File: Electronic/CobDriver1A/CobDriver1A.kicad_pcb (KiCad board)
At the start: 2 copper layers, 15 x 10 mm, 9 parts, among them J1 Conn02_Pin, J2 Conn02_Pin, U1 AL8860WT-7

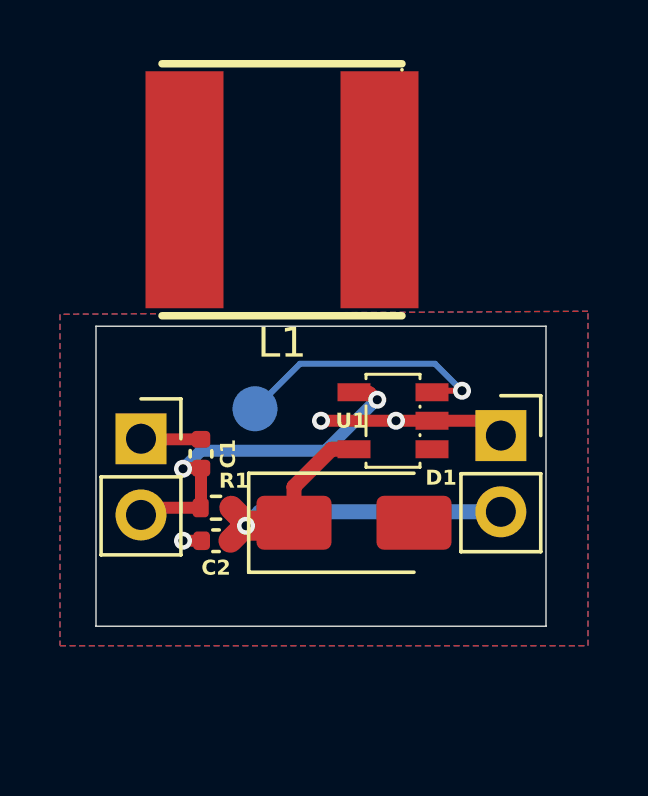
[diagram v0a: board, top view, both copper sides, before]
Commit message: CobDriver1A done
- Smaller inductor
- Bigger PCB
- BOM completed
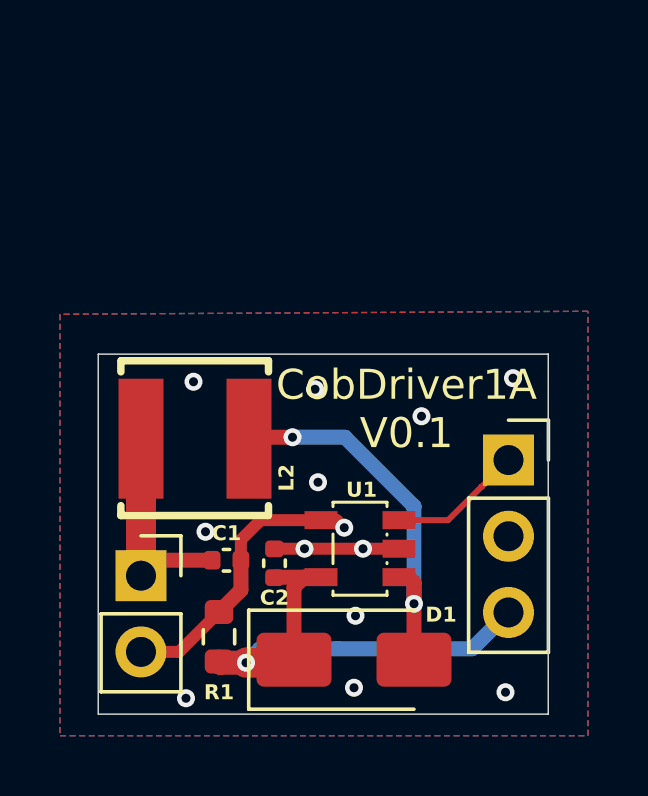
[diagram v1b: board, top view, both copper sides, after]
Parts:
- removed J2: Conn02_Pin, Connector_PinSocket_2.54mm:PinSocket_1x02_P2.54mm_Vertical
- removed L1: ABG08A40M560, lcsc:IND-SMD_L8.0-W8.0_ABG08A40
- removed TP1: TestPoint, TestPoint:TestPoint_Pad_D1.5mm
- added J3: Conn_01x03_Pin, Connector_PinSocket_2.54mm:PinSocket_1x03_P2.54mm_Vertical, F.Cu at (120.8, 60.0)
- added L2: LSXND5050YKL330MMG, lcsc:IND-SMD_L4.9-W4.9_LSXND5050, F.Cu at (110.4, 59.3)
- D1: value D -> MBRA140T3G
- R1: footprint Resistor_SMD:R_0402_1005Metric -> Resistor_SMD:R_0603_1608Metric
- moved D1 4.57 mm to (115.7, 66.7)
- moved J1 4.57 mm to (108.6, 63.9)
- moved U1 4.40 mm to (115.9, 63.0)
- moved R1 4.30 mm to (111.2, 65.9), turned to 90 degrees
- moved C1 3.65 mm to (111.5, 63.4), turned to 180 degrees
- moved C2 2.09 mm to (113.0, 63.5), turned to 90 degrees
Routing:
- net Net-(D1-A): track 0.00 -> 12.9 mm, vias 0 -> 2
- net Net-(J1-Pin_1): track 2.01 -> 7.18 mm
- net /PWM_COB: track 8.91 -> 4.55 mm, vias 1 -> 0
- net GND: track 6.82 -> 4.15 mm, vias 3 -> 12
- net /COB_SET: track 12.3 -> 10.0 mm, vias 2 -> 1
- net VCC: track 15.6 -> 17.1 mm
- added copper zone on In1.Cu, net GND
- added copper zone on In2.Cu, net GND
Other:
- board size 15 x 10 mm -> 15 x 12 mm
- copper layers 2 -> 4
- board text added: "12V + - PWM"
- board text added: "COB + -"
- board text added: "CobDriver1A V0.1"
